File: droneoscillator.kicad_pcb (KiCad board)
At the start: 2 copper layers, 29.5 x 114.3 mm, 44 parts, among them J1 Conn_01x02, J2 Conn_01x03, Q1 BC337, Q2 BC337, Q3 BC337, Q4 BC337, U1 NE5532

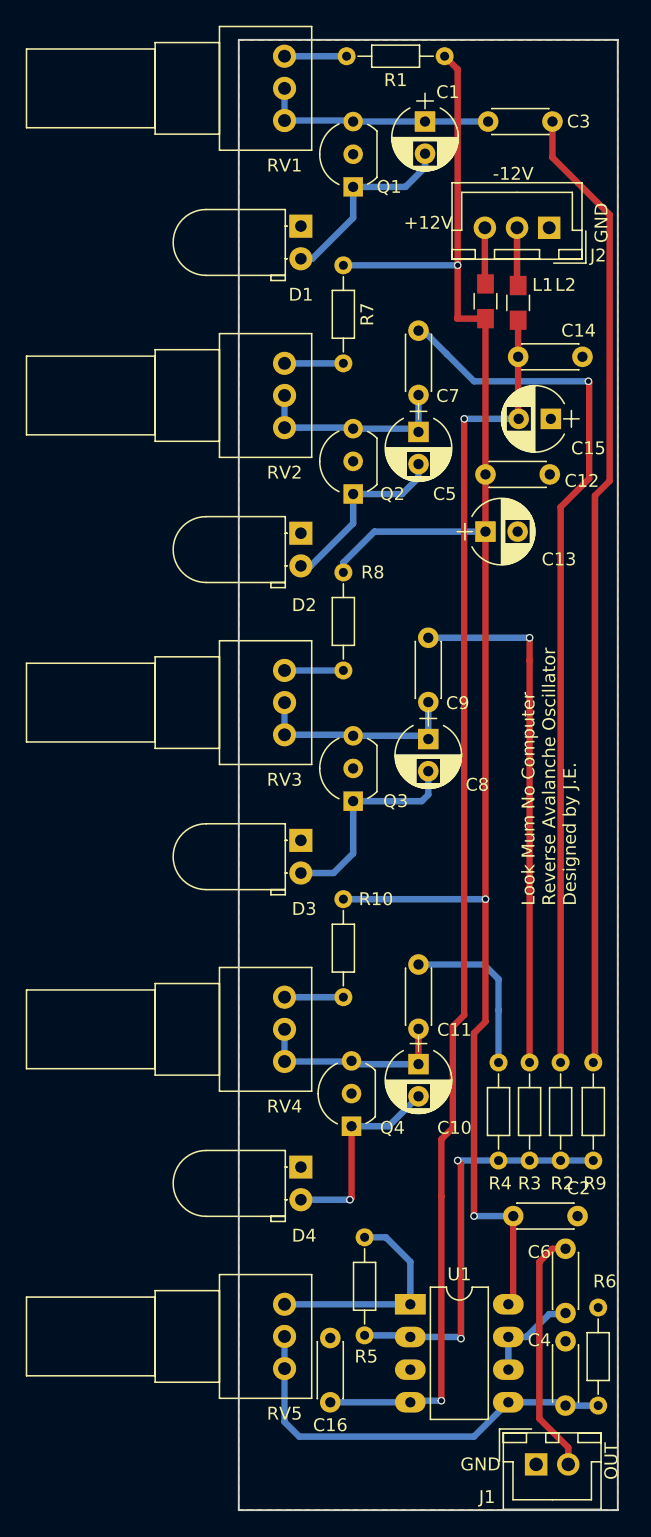
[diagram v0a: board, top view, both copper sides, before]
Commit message: update after prototype build, new PCB layout
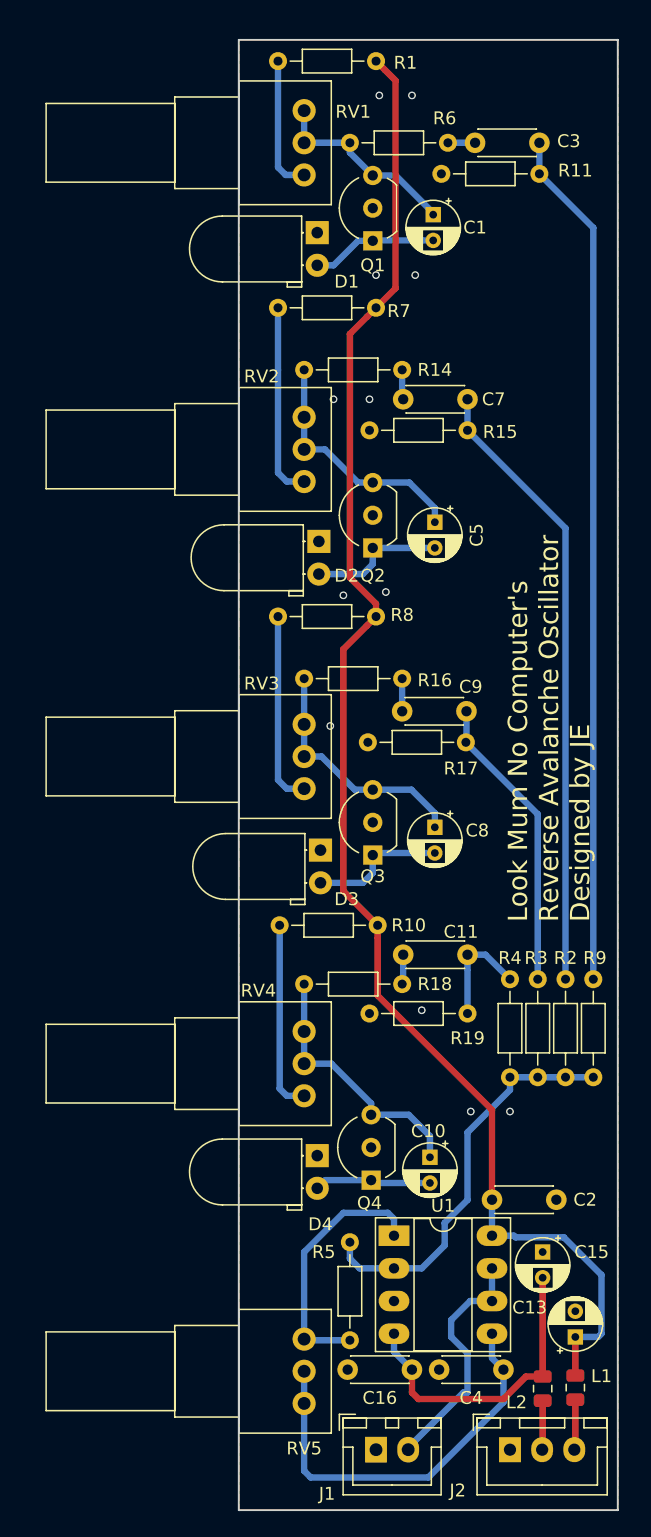
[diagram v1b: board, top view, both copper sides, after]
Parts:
- removed C12, C14: 100n, Capacitors_THT:C_Disc_D4.3mm_W1.9mm_P5.00mm
- removed C6: 1u, Capacitors_THT:C_Disc_D4.3mm_W1.9mm_P5.00mm
- added R11: 100K, Resistor_THT:R_Axial_DIN0204_L3.6mm_D1.6mm_P7.62mm_Horizontal, F.Cu at (154.7, 49.3)
- added R14: 10K, Resistor_THT:R_Axial_DIN0204_L3.6mm_D1.6mm_P7.62mm_Horizontal, F.Cu at (144.0, 64.5)
- added R15: 100K, Resistor_THT:R_Axial_DIN0204_L3.6mm_D1.6mm_P7.62mm_Horizontal, F.Cu at (149.1, 69.2)
- added R16: 10K, Resistor_THT:R_Axial_DIN0204_L3.6mm_D1.6mm_P7.62mm_Horizontal, F.Cu at (144.0, 88.5)
- added R17: 100K, Resistor_THT:R_Axial_DIN0204_L3.6mm_D1.6mm_P7.62mm_Horizontal, F.Cu at (149.0, 93.5)
- added R18: 10K, Resistor_THT:R_Axial_DIN0204_L3.6mm_D1.6mm_P7.62mm_Horizontal, F.Cu at (144.0, 112.3)
- added R19: 100K, Resistor_THT:R_Axial_DIN0204_L3.6mm_D1.6mm_P7.62mm_Horizontal, F.Cu at (149.1, 114.6)
- C1, C10, C5, C8: value 10u -> 2u2; footprint Capacitors_THT:CP_Radial_D5.0mm_P2.50mm -> Capacitor_THT:CP_Radial_D4.0mm_P2.00mm
- C11, C3, C7, C9: value 1u -> 100n; footprint Capacitors_THT:C_Disc_D4.3mm_W1.9mm_P5.00mm -> Capacitor_THT:C_Disc_D4.3mm_W1.9mm_P5.00mm
- C13, C15: footprint Capacitors_THT:CP_Radial_D5.0mm_P2.50mm -> Capacitor_THT:CP_Radial_D4.0mm_P2.00mm
- C16, C2: footprint Capacitors_THT:C_Disc_D4.3mm_W1.9mm_P5.00mm -> Capacitor_THT:C_Disc_D4.3mm_W1.9mm_P5.00mm
- C4: value 1u -> 1n; footprint Capacitors_THT:C_Disc_D4.3mm_W1.9mm_P5.00mm -> Capacitor_THT:C_Disc_D4.3mm_W1.9mm_P5.00mm
- J1: footprint Connectors_JST:JST_XH_B02B-XH-A_02x2.50mm_Straight -> Connector_JST:JST_XH_B02B-XH-A_1x02_P2.50mm_Vertical
- J2: footprint Connectors_JST:JST_XH_B03B-XH-A_03x2.50mm_Straight -> Connector_JST:JST_XH_B03B-XH-A_1x03_P2.50mm_Vertical
- L1, L2: footprint Inductors_SMD:L_0805_HandSoldering -> Inductor_SMD:L_0805_2012Metric
- Q1, Q2, Q3, Q4: footprint TO_SOT_Packages_THT:TO-92_Inline_Wide -> Package_TO_SOT_THT:TO-92_Inline_Wide
- R1, R10, R2, R3, R4, R5, R7, R8, R9: footprint Resistors_THT:R_Axial_DIN0204_L3.6mm_D1.6mm_P7.62mm_Horizontal -> Resistor_THT:R_Axial_DIN0204_L3.6mm_D1.6mm_P7.62mm_Horizontal
- R6: value 1M -> 10K; footprint Resistors_THT:R_Axial_DIN0204_L3.6mm_D1.6mm_P7.62mm_Horizontal -> Resistor_THT:R_Axial_DIN0204_L3.6mm_D1.6mm_P7.62mm_Horizontal
- RV1, RV2, RV3, RV4, RV5: value 10K -> 100K
- U1: footprint Package_DIP:DIP-8_W7.62mm_LongPads -> Package_DIP:DIP-8_W7.62mm_Socket_LongPads
- moved J2 95.0 mm to (152.4, 148.5), turned to 0 degrees
- moved R6 91.3 mm to (147.6, 46.9), turned to 180 degrees
- moved L1 84.7 mm to (157.5, 143.6), turned to 90 degrees
- moved L2 84.4 mm to (154.9, 143.7), turned to 90 degrees
- moved C15 64.8 mm to (154.9, 133.1), turned to 270 degrees
- moved C13 63.0 mm to (157.5, 139.7), turned to 90 degrees
- moved J1 12.5 mm to (142.0, 148.5)
- moved R5 8.08 mm to (140.0, 140.0), turned to 90 degrees
- moved C10 7.29 mm to (146.2, 125.7)
- moved C1 7.27 mm to (146.4, 52.5)
- moved C5 7.13 mm to (146.6, 76.4)
- moved C8 6.88 mm to (146.6, 100.1)
- moved C16 6.84 mm to (144.8, 142.2), turned to 180 degrees
- moved C7 6.55 mm to (149.1, 66.8), turned to 180 degrees
- moved R4 6.54 mm to (152.4, 119.5)
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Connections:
- C11 pad 2: Net-(C10-Pad1) -> Net-(C11-Pad2)
- C3 pad 2: Net-(C1-Pad1) -> Net-(C3-Pad2)
- C7 pad 2: Net-(C5-Pad1) -> Net-(C7-Pad2)
- C9 pad 2: Net-(C8-Pad1) -> Net-(C9-Pad2)
- J1 pad 2: Net-(C6-Pad1) -> Net-(J1-Pad2)
- R6 pad 1: GND -> Net-(C3-Pad2)
- R6 pad 2: Net-(C4-Pad1) -> Net-(C1-Pad1)
- RV1 pad 1: Net-(R1-Pad2) -> Net-(C1-Pad1)
- RV1 pad 3: Net-(C1-Pad1) -> Net-(R1-Pad2)
- RV2 pad 1: Net-(R7-Pad2) -> Net-(C5-Pad1)
- RV2 pad 3: Net-(C5-Pad1) -> Net-(R7-Pad2)
- RV3 pad 1: Net-(R8-Pad2) -> Net-(C8-Pad1)
- RV3 pad 3: Net-(C8-Pad1) -> Net-(R8-Pad2)
- RV4 pad 1: Net-(R10-Pad2) -> Net-(C10-Pad1)
- RV4 pad 3: Net-(C10-Pad1) -> Net-(R10-Pad2)
- U1 pad 6: Net-(C6-Pad2) -> Net-(J1-Pad2)
- U1 pad 7: Net-(C6-Pad2) -> Net-(J1-Pad2)
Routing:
- net -12VA: track 97.7 -> 23.9 mm, vias 2 -> 0
- net /OscB: track 68.7 -> 48.2 mm, vias 1 -> 0
- net Net-(C6-Pad1): track 19.1 -> 0.00 mm
- net Net-(J1-Pad2): track 0.00 -> 19.0 mm
- net /OscC: track 40.9 -> 23.2 mm, vias 1 -> 0
- net +12V: track 136.0 -> 119.6 mm, vias 3 -> 0
- net Net-(R7-Pad2): track 4.57 -> 14.4 mm
- net Net-(R8-Pad2): track 4.57 -> 14.3 mm
- net Net-(R10-Pad2): track 4.57 -> 14.1 mm
- net /OscA: track 75.5 -> 66.8 mm
- net Net-(C6-Pad2): track 7.98 -> 0.00 mm
- net Net-(C10-Pad2): track 15.7 -> 9.12 mm, vias 1 -> 0
- net Net-(C8-Pad2): track 16.6 -> 10.7 mm
- net Net-(C1-Pad2): track 15.1 -> 9.82 mm
- net Net-(R1-Pad2): track 4.83 -> 9.83 mm
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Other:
- board text added: "Look Mum No Computer's Reverse Avalanche Oscillator Designed by JE"
- board text removed: "+12V"
- board text removed: "-12V"
- board text removed: "GND"
- board text removed: "Look Mum No Computer Reverse Avalanche Oscillator Designed by J.E."
- board text removed: "OUT"

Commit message: schematic bugfix, minor changes to PCB
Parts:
- C4: value 1n -> 100n
- D1, D2, D3, D4: footprint LEDs:LED_D5.0mm_Horizontal_O1.27mm_Z3.0mm -> LED_THT:LED_D5.0mm_Horizontal_O1.27mm_Z3.0mm
- RV1, RV2, RV3, RV4, RV5: footprint Potentiometers:Potentiometer_Alps_RK097_Single_Vertical -> Potentiometer_THT:Potentiometer_Alps_RK097_Single_Horizontal
- moved C4 20.1 mm to (132.8, 148.6), turned to 0 degrees
- moved C16 1.52 mm to (146.3, 142.2), turned to 0 degrees
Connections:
- RV5 pad 1: Net-(R5-Pad1) -> Net-(C4-Pad1)
- RV5 pad 3: Net-(C4-Pad1) -> Net-(R5-Pad1)
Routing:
- net +12V: track 119.6 -> 165.9 mm, vias 0 -> 3
- net Net-(R5-Pad1): track 20.1 -> 24.0 mm
- net Net-(C4-Pad1): track 31.6 -> 27.8 mm
- net -12VA: track 23.9 -> 22.1 mm
- net Net-(J1-Pad2): track 19.0 -> 18.4 mm
- net GND: vias 12 -> 0
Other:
- board text added: "Look Mum No Computer's Reverse Avalanche Oscillator Adapted by JE"
- board text removed: "Look Mum No Computer's Reverse Avalanche Oscillator Designed by JE"

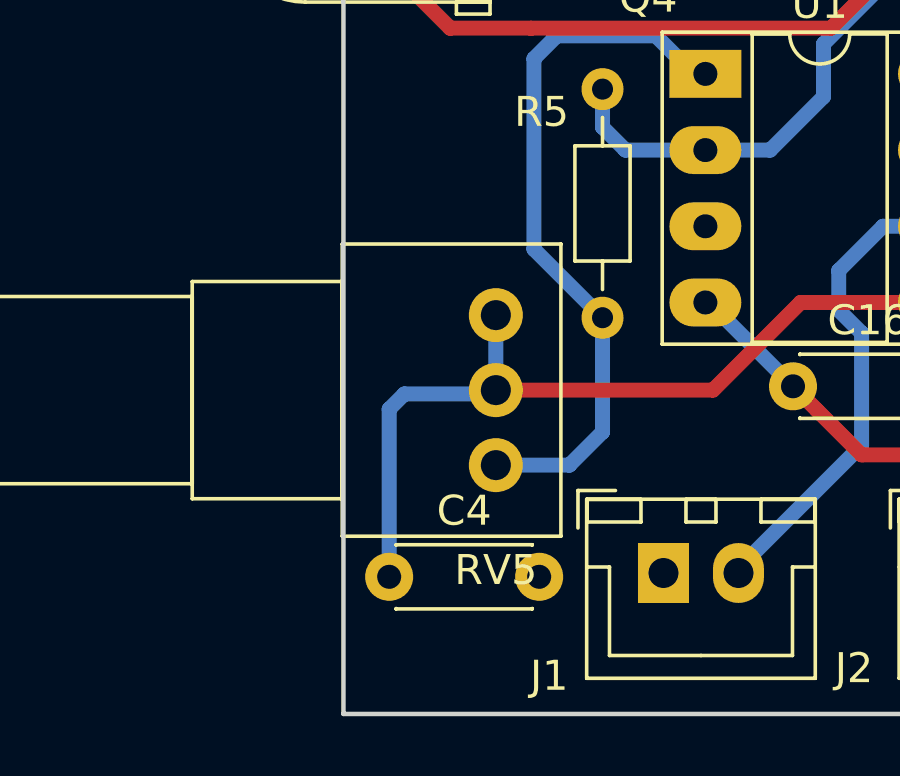
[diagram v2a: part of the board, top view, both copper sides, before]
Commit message: silkscreen bugfix
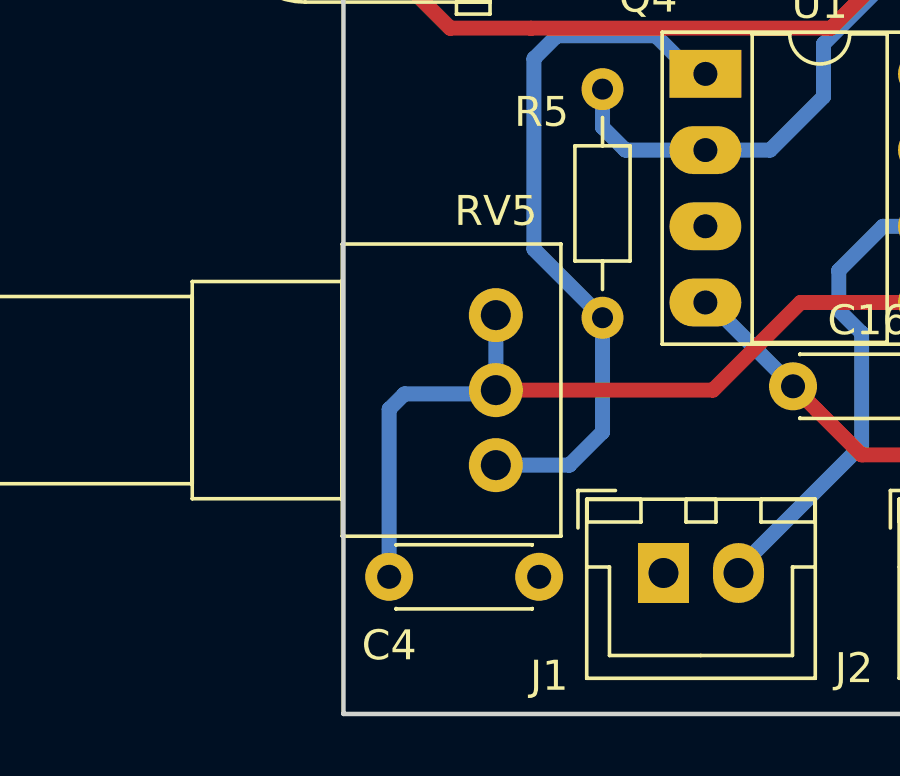
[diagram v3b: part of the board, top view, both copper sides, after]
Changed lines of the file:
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@@
     (descr "C, Disc series, Radial, pin pitch=5.00mm, , diameter*width=4.3*1.9mm^2, Capacitor, http://www.vishay.com/docs/45233/krseries.pdf")
     (tags "C Disc series Radial pin pitch 5.00mm  diameter 4.3mm width 1.9mm Capacitor")
-    (fp_text reference C4 (at 2.5 -2.2) (layer F.SilkS)
+    (fp_text reference C4 (at 0 2.286) (layer F.SilkS)
       (effects (font (size 1 1) (thickness 0.15)))
     )
@@
     (descr "Potentiometer, horizontal, Alps RK097 Single, http://www.alps.com/prod/info/E/HTML/Potentiometer/RotaryPotentiometers/RK097/RK097_list.html")
     (tags "Potentiometer horizontal Alps RK097 Single")
-    (fp_text reference RV5 (at 0 -8.5 180) (layer F.SilkS)
+    (fp_text reference RV5 (at 0 3.469 180) (layer F.SilkS)
       (effects (font (size 1 1) (thickness 0.15)))
     )
@@
       (at (xyz 0 0 0))
       (scale (xyz 1 1 1))
+      (rotate (xyz 0 0 0))
+    )
+    (model ${KISYS3DMOD}/Potentiometer_THT.3dshapes/Potentiometer_Alps_RK097_Single_Vertical.wrl
+      (at (xyz 0 0 0))
+      (scale (xyz 0.4 0.4 0.4))
       (rotate (xyz 0 0 0))
     )
@@
       (rotate (xyz 0 0 0))
     )
+    (model ${KISYS3DMOD}/Potentiometer_THT.3dshapes/Potentiometer_Alps_RK097_Single_Vertical.wrl
+      (at (xyz 0 0 0))
+      (scale (xyz 0.4 0.4 0.4))
+      (rotate (xyz 0 0 0))
+    )
   )
   (module Potentiometer_THT:Potentiometer_Alps_RK097_Single_Horizontal locked (layer F.Cu)
@@
       (at (xyz 0 0 0))
       (scale (xyz 1 1 1))
+      (rotate (xyz 0 0 0))
+    )
+    (model ${KISYS3DMOD}/Potentiometer_THT.3dshapes/Potentiometer_Alps_RK097_Single_Vertical.wrl
+      (at (xyz 0 0 0))
+      (scale (xyz 0.4 0.4 0.4))
       (rotate (xyz 0 0 0))
     )
@@
       (rotate (xyz 0 0 0))
     )
+    (model ${KISYS3DMOD}/Potentiometer_THT.3dshapes/Potentiometer_Alps_RK097_Single_Vertical.wrl
+      (at (xyz 0 0 0))
+      (scale (xyz 0.4 0.4 0.4))
+      (rotate (xyz 0 0 0))
+    )
   )
   (module Potentiometer_THT:Potentiometer_Alps_RK097_Single_Horizontal locked (layer F.Cu)
@@
       (rotate (xyz 0 0 0))
     )
+    (model ${KISYS3DMOD}/Potentiometer_THT.3dshapes/Potentiometer_Alps_RK097_Single_Vertical.wrl
+      (at (xyz 0 0 0))
+      (scale (xyz 0.4 0.4 0.4))
+      (rotate (xyz 0 0 0))
+    )
